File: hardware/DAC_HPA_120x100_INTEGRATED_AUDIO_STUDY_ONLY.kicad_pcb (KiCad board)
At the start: 4 copper layers, 120 x 100 mm, 544 parts, among them J101 GCT USB4105-GF-A, J201 PCB pads (no component), J202 PCB pads (no component), J701 G-Switch GT-3321667P-01, J702 HRO PJ-332A-6A, K601 TLP3545A, K602 TLP3545A, K603 TLP3545A, K604 TLP3545A, Q207 AO3400A, Q502 AO3400A, Q503 AO3400A, Q504 AO3400A, Q505 AO3400A, Q506 AO3400A, Q507 MMBT3904, Q612 MMBT3904, Q614 MMBT3904, Q616 AO3400A, Q617 AO3400A, Q618 2N7002, Q619 AO3400A, Q620 AO3400A, Q621 2N7002, Q622 AO3400A, Q623 MMBT3904, Q624 MMBT3904, Q625 MMBT3904, Q626 MMBT3904, Q627 MMBT3904, U101 ST USBLC6-2SC6, U102 TI TPS25200DRVR, U103 TI TPD2E2U06DRLR, U201 CH32V307RCT6, U202 AGRV2KQ32, U205 74LVC1G157, U206 74LVC1G11, U208 74LVC3G34, U301 ES9018K2M, U302 3.3 V, 250 mA, U303 1.300 V (R533/R534), U401 OPA1622IDRCR, U402 OPA1622IDRCR, U403 OPA2210IDGKR, U404 OPA2210IDGKR, U501 +3.85 / -3.72 V, U502 3.3 V, 150 mA, U503 TI TPS259621DDAR, U504 3.3 V, 1 A, U505 TI TMUX1101DBVR, U603 TLV1704, U604 OPA2333, U605 TLV3402, U606 TLV1704, U607 74AUP1G17, U608 74LVC1G74, U609 TLV1704, U610 TLV1704, U611 TLV1704, U612 TLV1704, U613 TLV3402, U614 TLV3402, U615 TLV3402, U616 TLV3402, U617 TLV3402, U618 TLV3402, U619 TLV3402, U620 TLV3402, U621 SN74AUP2G17DCKR, X201 80.000 MHz, X202 49.152 MHz, X203 45.1584 MHz, Y201 8 MHz

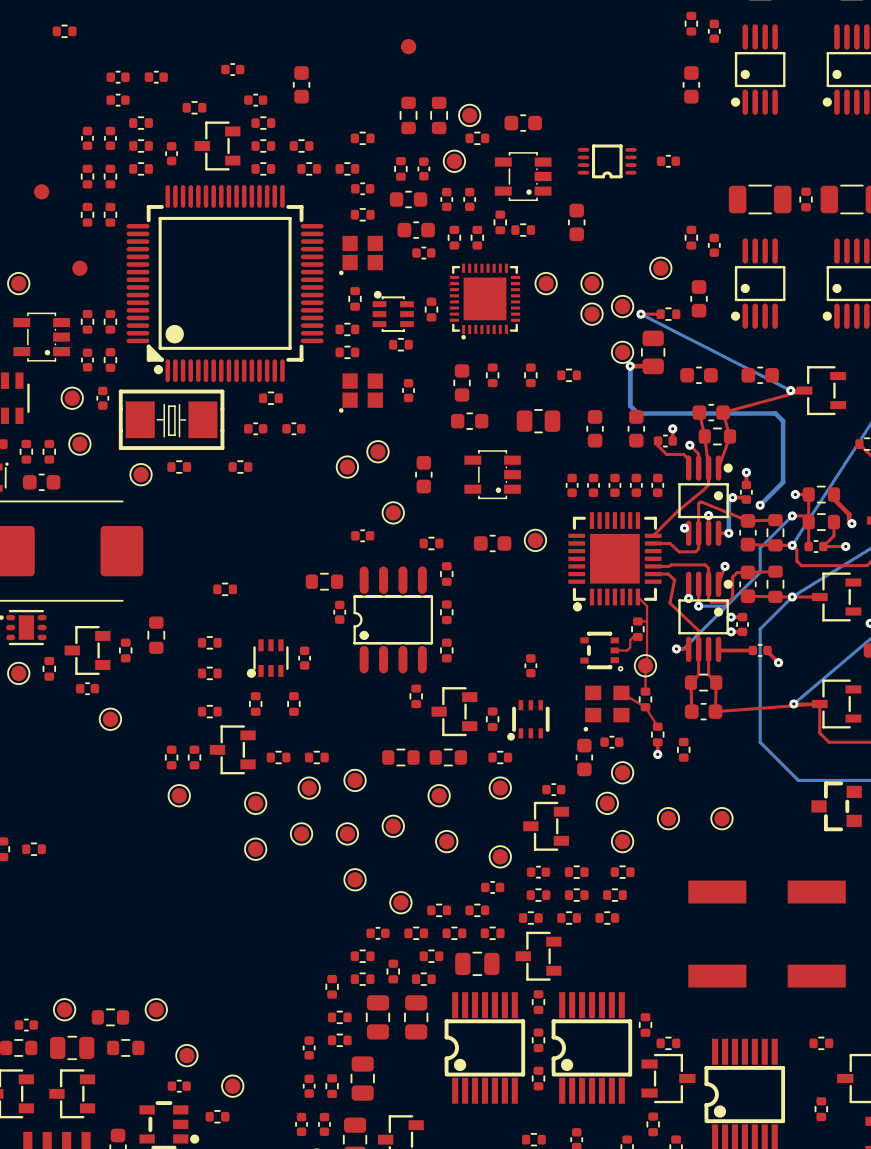
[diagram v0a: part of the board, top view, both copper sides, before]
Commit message: Route DAC core and local supplies in manual audio study
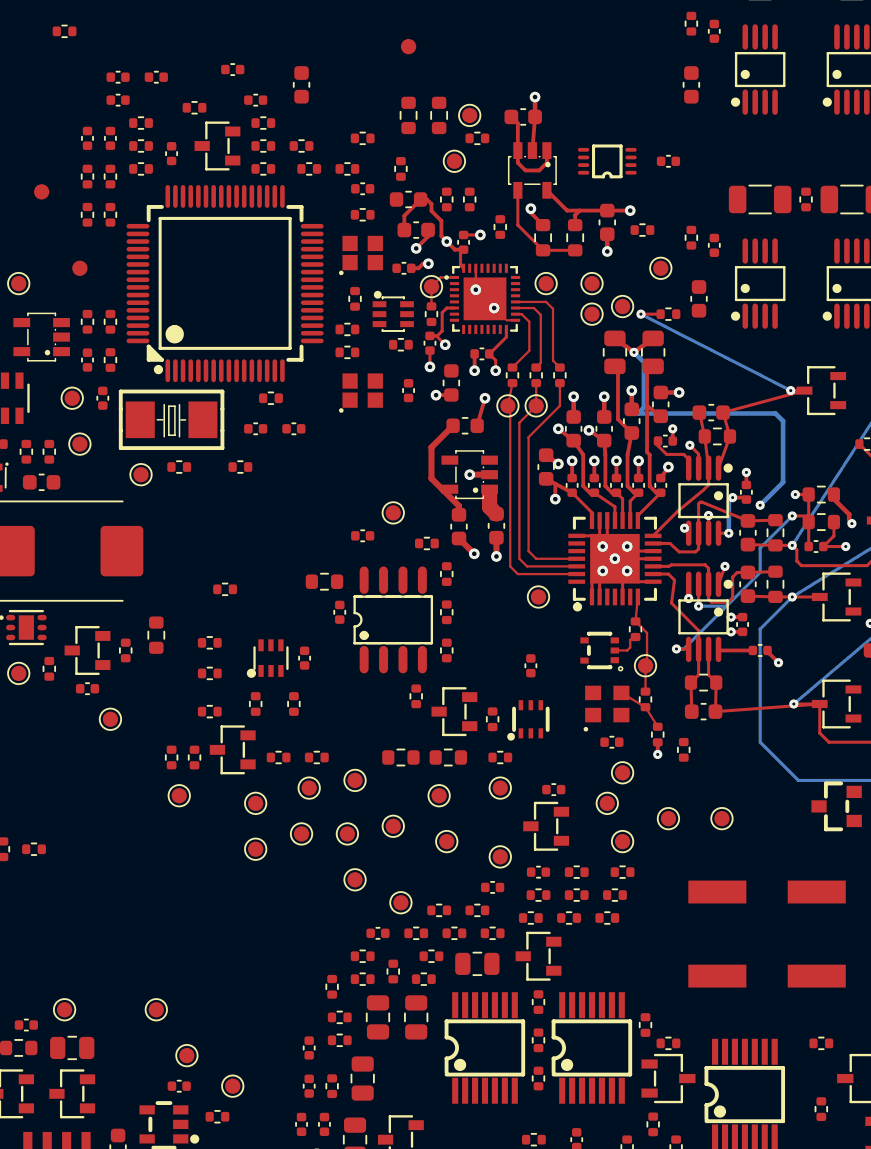
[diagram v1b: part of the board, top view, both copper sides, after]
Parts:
- moved R533 60.6 mm to (87.9, 60.0), turned to -90 degrees
- moved R534 58.3 mm to (85.8, 60.0), turned to 90 degrees
- moved C312 19.2 mm to (86.0, 75.0)
- moved TP746 16.9 mm to (85.5, 83.5)
- moved TP716 13.0 mm to (85.3, 71.0)
- moved C214 12.7 mm to (81.8, 67.6), turned to 180 degrees
- moved TP712 11.4 mm to (78.5, 63.2)
- moved C440 10.8 mm to (89.8, 72.5), turned to 90 degrees
- moved C215 9.75 mm to (78.4, 66.9), turned to -90 degrees
- moved TP715 8.98 mm to (83.5, 71.0)
- moved C439 8.92 mm to (87.8, 72.5), turned to 90 degrees
- moved R305 7.80 mm to (92.3, 59.5)
- moved R302 6.73 mm to (90.5, 67.5), turned to -90 degrees
- moved C301 5.81 mm to (82.8, 78.8), turned to -90 degrees
- moved C213 3.01 mm to (80.6, 60.3)
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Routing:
- net 1V3: track 0.00 -> 37.8 mm, vias 0 -> 2
- net GND: track 51.8 -> 89.5 mm, vias 37 -> 65
- net N2_V33_CPLD: track 0.00 -> 26.9 mm, vias 0 -> 3
- net DVCC: track 0.00 -> 18.3 mm, vias 0 -> 2
- net VCCA: track 0.00 -> 17.3 mm, vias 0 -> 2
- net BCLK: track 0.00 -> 16.6 mm
- net LRCLK: track 0.00 -> 15.9 mm
- net SDATA: track 0.00 -> 15.2 mm
- net AVCC_L: track 0.00 -> 12.5 mm
- net AVCC_R: track 0.00 -> 11.3 mm
- net 3V3A: track 29.5 -> 39.9 mm
- net N3_1V3_FB: track 0.00 -> 6.71 mm
- net N2_SDATA_SRC: track 0.00 -> 6.66 mm
- net 3V3D: track 0.00 -> 6.29 mm
- net N2_LRCLK_SRC: track 0.00 -> 5.40 mm
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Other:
- board text added: "INTEGRATED AUDIO + DAC CORE / MANUAL ROUTE STUDY — NO PCBA RELEASE"
- board text removed: "INTEGRATED AUDIO / MANUAL ROUTE STUDY — NO PCBA RELEASE"

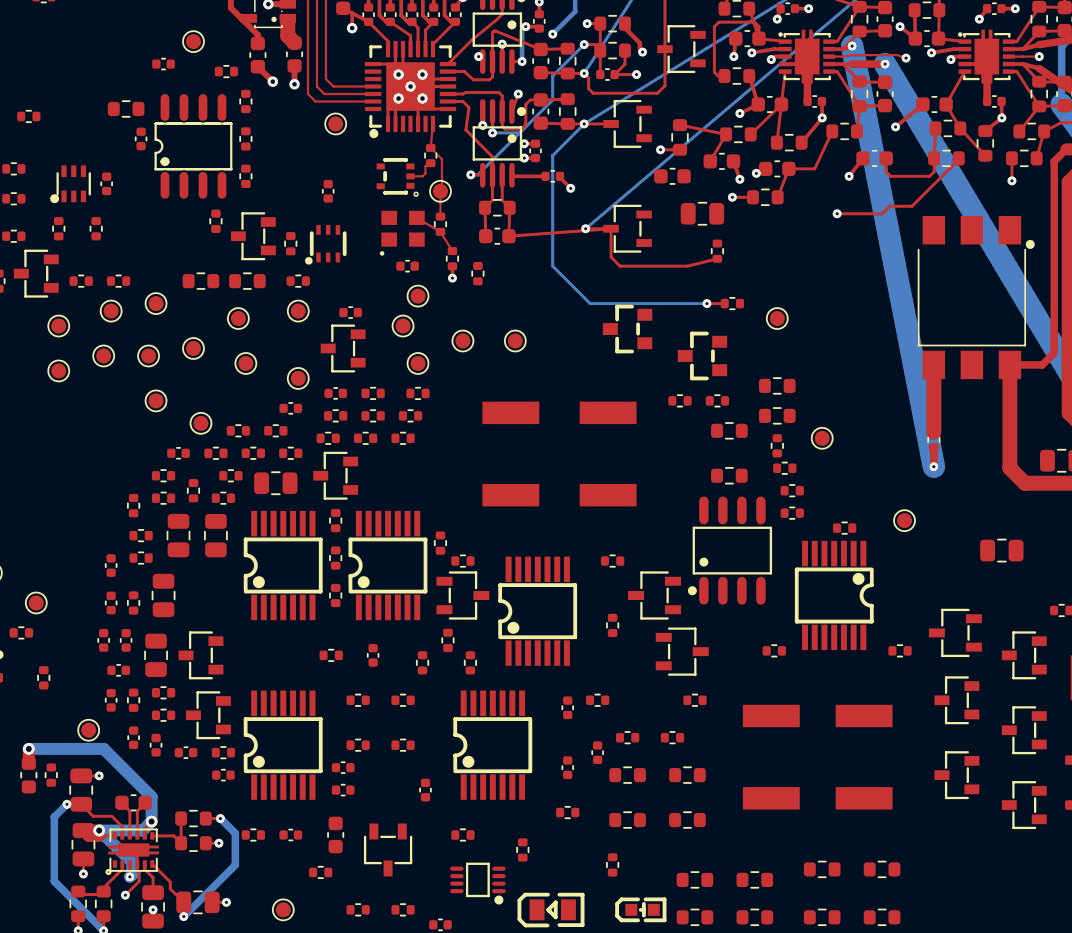
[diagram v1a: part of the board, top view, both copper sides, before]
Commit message: Route U610 timer cluster and bound local PCB clearances
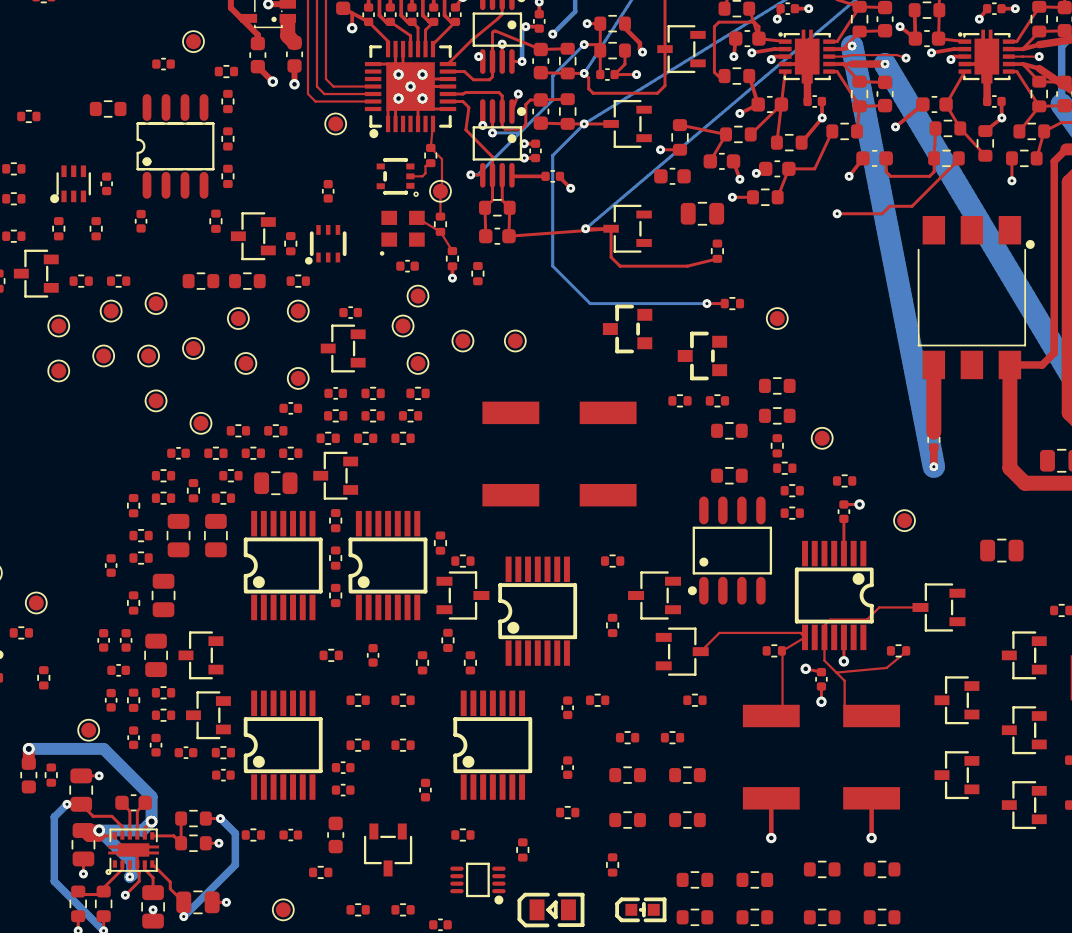
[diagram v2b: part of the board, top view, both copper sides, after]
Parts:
- moved C637 49.3 mm to (119.5, 109.4)
- moved C638 15.7 mm to (118.0, 120.6), turned to -90 degrees
- moved C625 5.50 mm to (72.5, 90.0)
- moved R644 3.15 mm to (119.5, 107.3)
- moved Q626 2.02 mm to (125.8, 115.8)
- moved R675 1.20 mm to (78.3, 84.5)
- moved R676 1.20 mm to (78.3, 82.0)
- moved R677 1.20 mm to (70.3, 82.5)
- moved R679 1.20 mm to (78.3, 87.0)
- moved U605 1.20 mm to (74.8, 85.0)
- moved C634 0.50 mm to (121.3, 125.8)
- moved R923 0.10 mm to (123.1, 118.7)
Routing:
- net N6_TLN_R: track 0.00 -> 16.8 mm
- net N6_TLP_R: track 0.00 -> 13.1 mm
- net GND: track 89.5 -> 96.8 mm, vias 65 -> 69
- net VNEG: track 23.0 -> 28.4 mm, vias 2 -> 4
- net VPOS: track 66.7 -> 69.0 mm

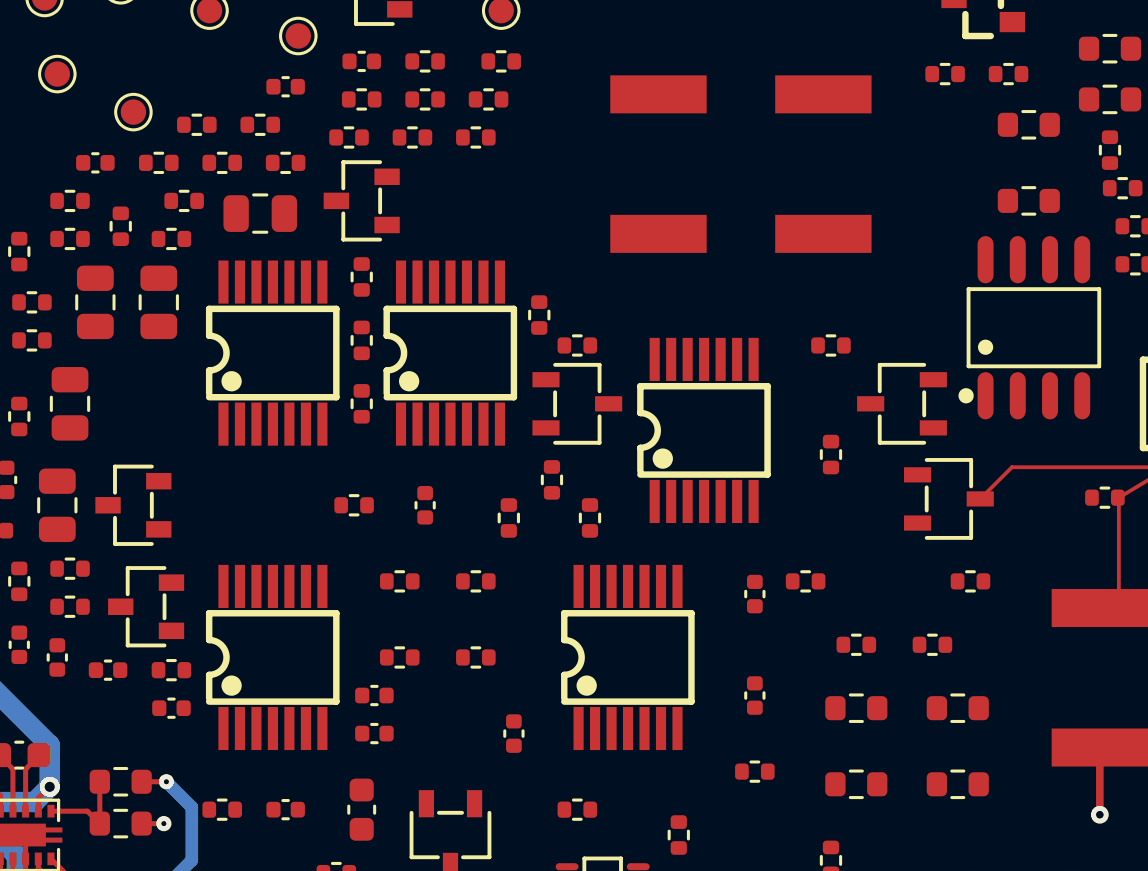
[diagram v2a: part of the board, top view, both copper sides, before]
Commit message: Localize U604 supply bypass on integrated board
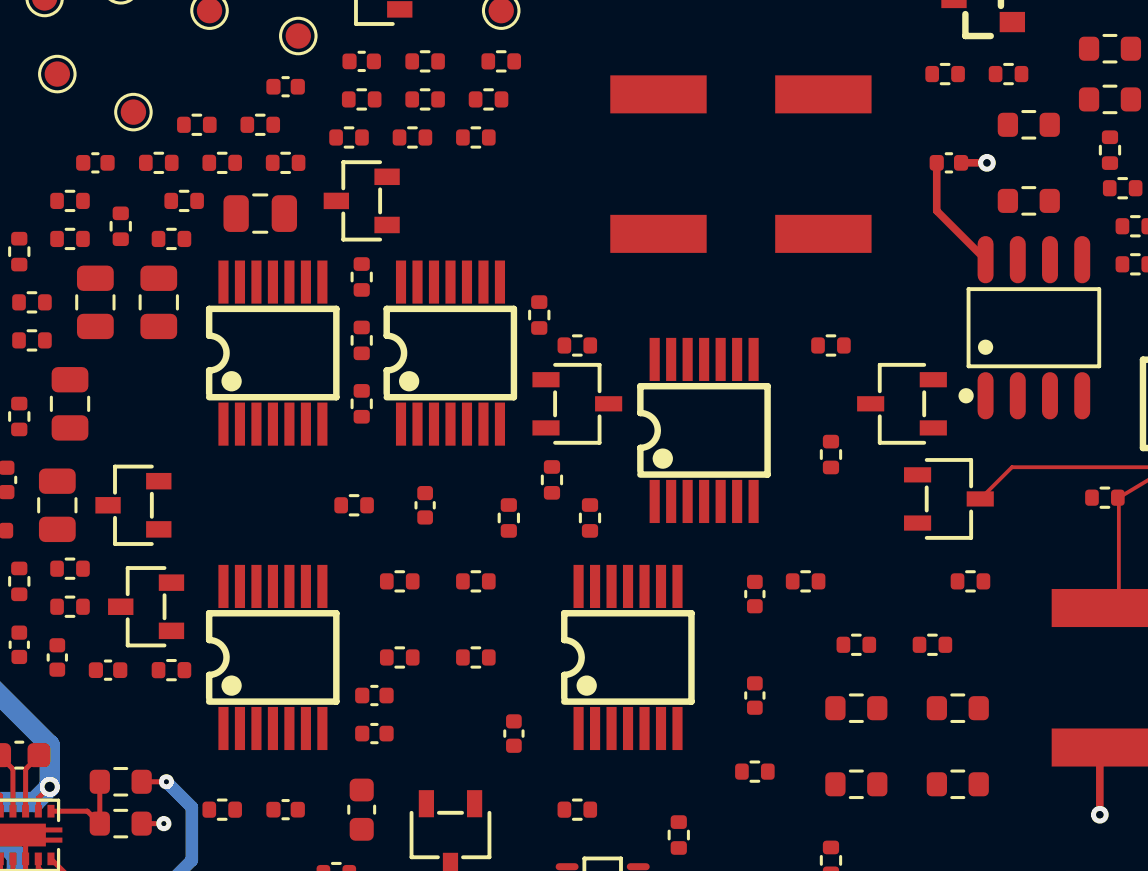
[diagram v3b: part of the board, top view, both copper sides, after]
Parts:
- moved C622 37.4 mm to (108.7, 105.5)
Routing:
- net 3V3D: track 6.29 -> 10.9 mm
- net GND: track 96.8 -> 97.9 mm, vias 69 -> 70

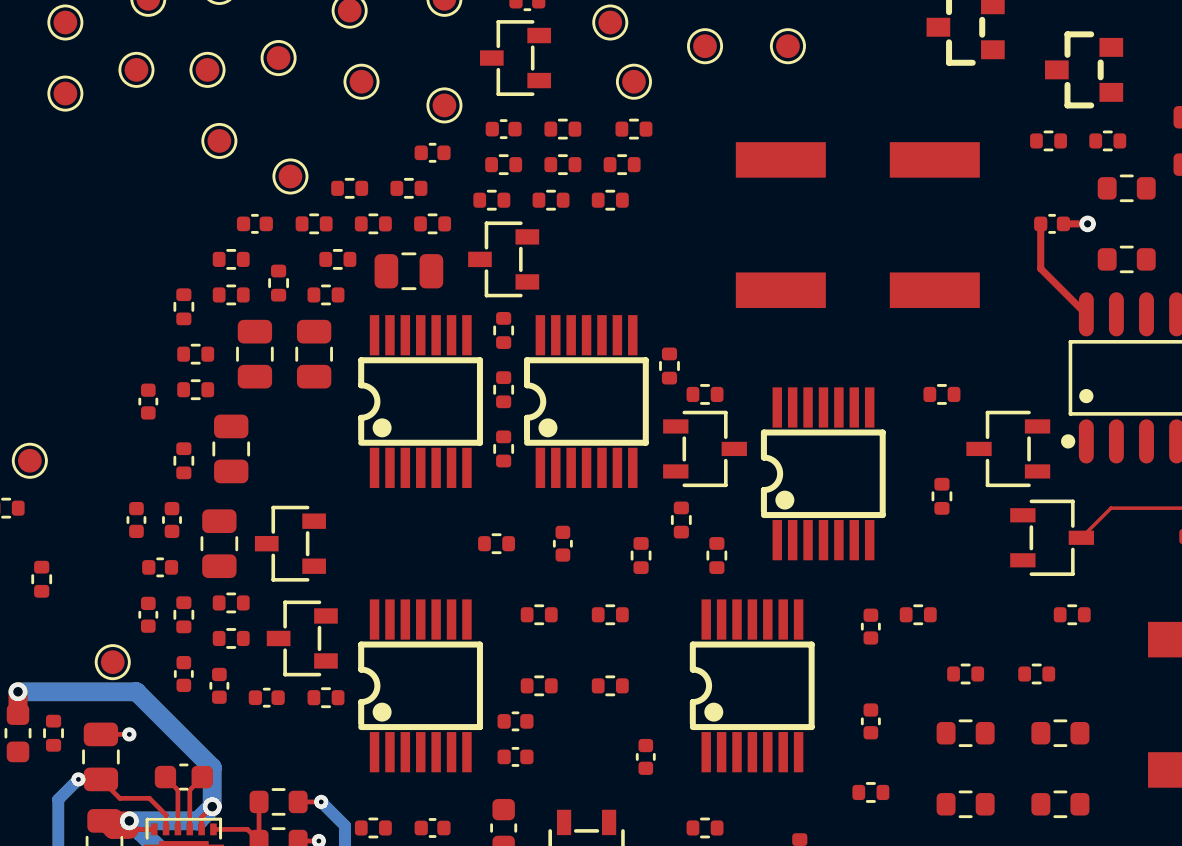
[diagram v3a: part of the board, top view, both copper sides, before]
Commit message: Route U609 timer cluster and record discharge model hold
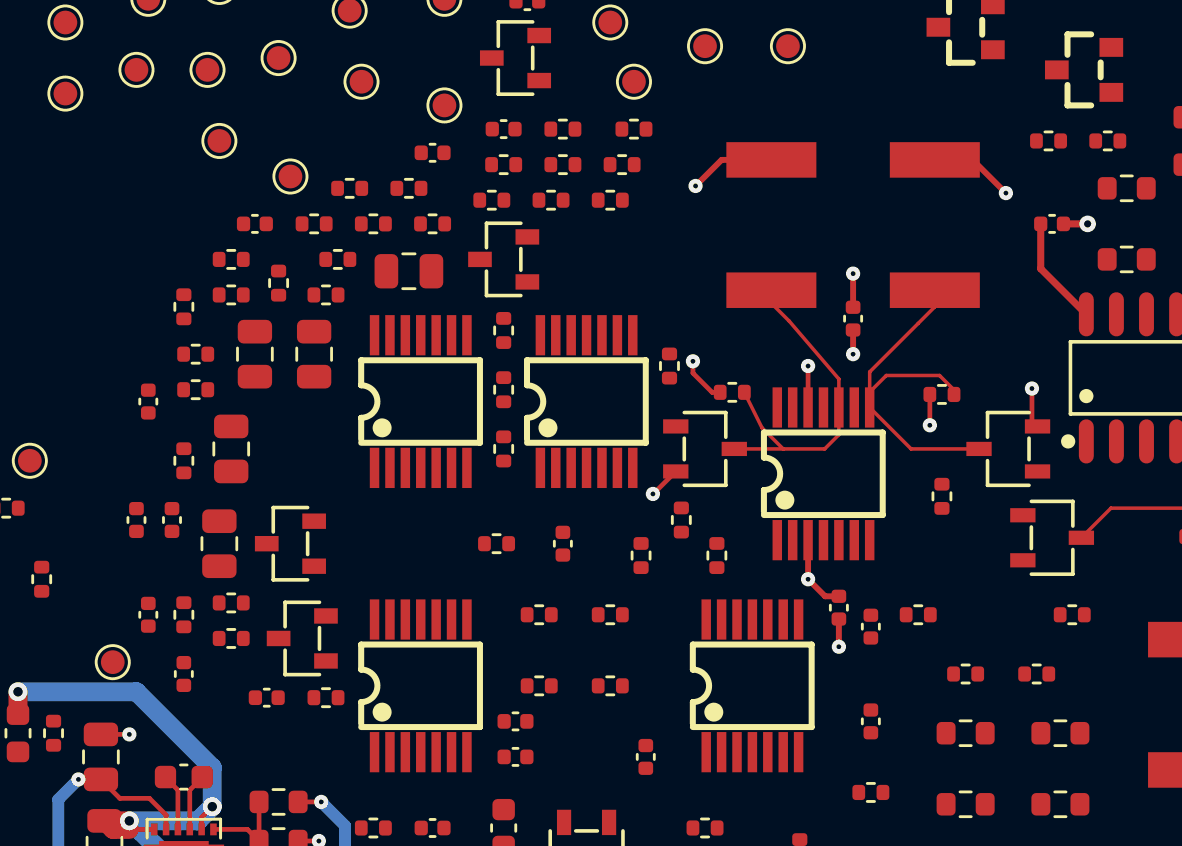
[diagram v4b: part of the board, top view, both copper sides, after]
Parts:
- moved C636 31.1 mm to (100.2, 109.5), turned to 90 degrees
- moved C635 26.4 mm to (99.7, 121.7), turned to -90 degrees
- moved R921 1.15 mm to (95.2, 112.6)
- moved C632 0.40 mm to (96.8, 105.5)
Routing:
- net VPOS: track 69.0 -> 93.6 mm, vias 8 -> 11
- net N6_TLP_L: track 0.00 -> 15.7 mm
- net N6_TLN_L: track 0.00 -> 14.8 mm
- net GND: track 97.9 -> 110.7 mm, vias 70 -> 76
- net VNEG: track 28.4 -> 33.3 mm, vias 4 -> 6

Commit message: Adopt two reviewed low-speed routing assist paths
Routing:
- net N7_LEDR_A: track 0.00 -> 4.65 mm
- net N2_AUD_EN_MCU: track 0.00 -> 4.29 mm
